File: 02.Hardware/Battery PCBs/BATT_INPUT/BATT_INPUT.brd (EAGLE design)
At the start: 26 x 30.6 mm, 39 parts, among them J1 70AAJ-4-M0, J4 DX07S016JA1R1500, U1 AT24C16D-STUM-T, U5 BQ24075, U9 Value

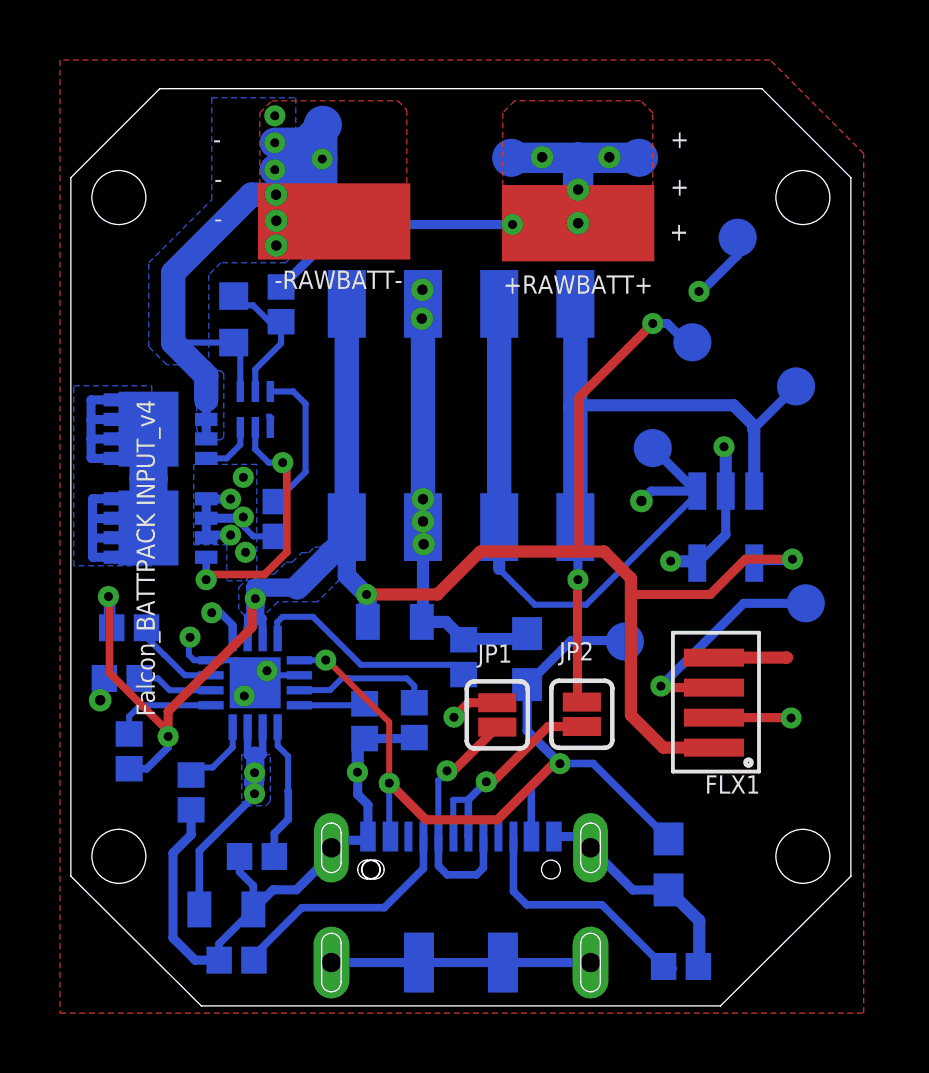
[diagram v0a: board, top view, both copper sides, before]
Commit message: Cambios revisados con David
Revision de los pcbs de la bateria.

En el DCDC se añade un diode Clamp (bat54s) en la medicion de la tension de salida.
Actualizacion de la BOM a v8.
Documentos de Cambios de versiones
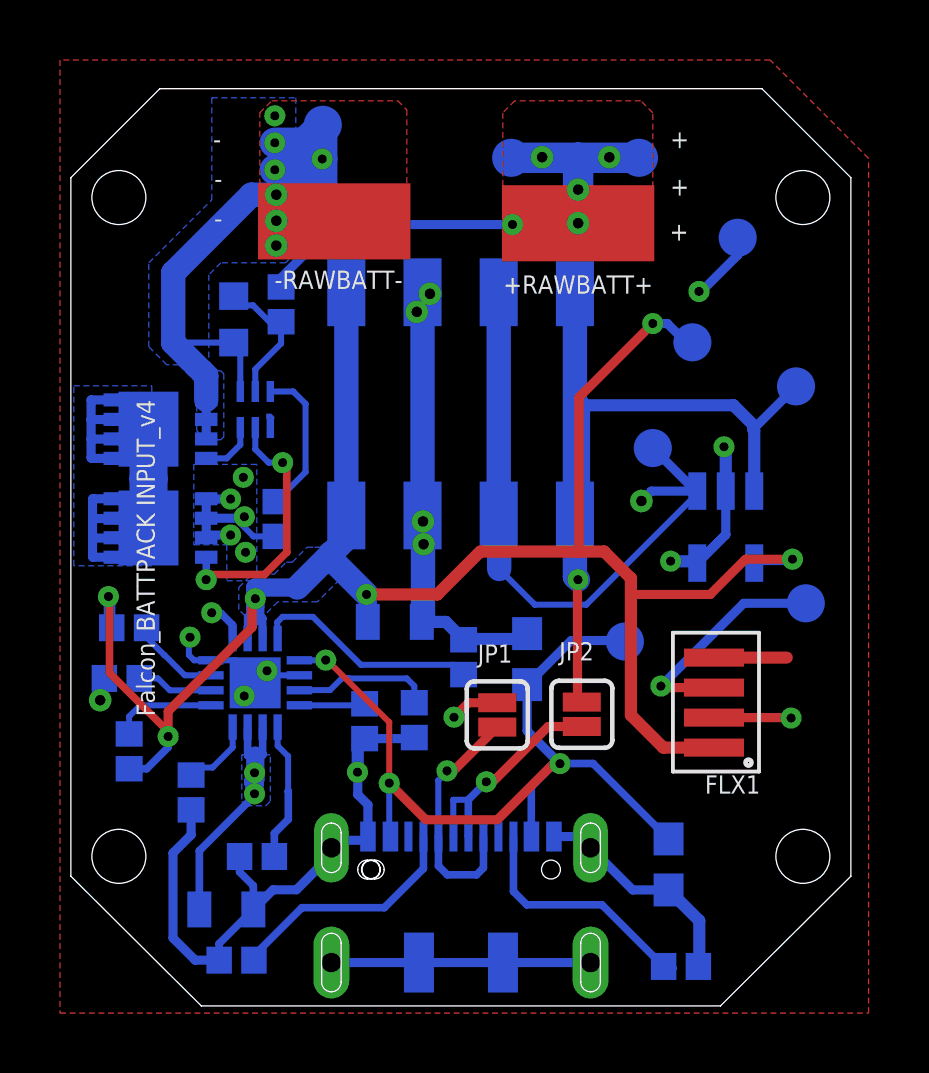
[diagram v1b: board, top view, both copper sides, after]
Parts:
- JP1, JP2: value JUMPER-SMT_2_NC_PASTE_SILK -> JUMPER-SMT_2_NO_SILK; device SparkFun-Jumpers:SMT-JUMPER_2_NC_PASTE_SILK -> SparkFun-Jumpers:SMT-JUMPER_2_NO_SILK
- moved J1 0.39 mm to (60.2, 57.2), turned to 180 degrees
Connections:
- net D+: now also J1.4, J1.5; no longer J1.1, J1.8
- net D-: now also J1.3, J1.6; no longer J1.2, J1.7
- net GND: now also J1.2, J1.7; no longer J1.3, J1.6
- net VSYS: now also J1.1, J1.8; no longer J1.4, J1.5
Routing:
- net D+: track 23.9 -> 30.0 mm
- net GND: track 73.9 -> 75.7 mm, vias 18 -> 17

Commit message: Review general antes de produccion
Se modifica:
R13 --> El sensado de vosense estaba tarado para 3.3v en vez de 3v de vsupply
R15 --> Se baja el valor porque  no hace falta que sea tan alta
C10 --> Error de valor 470n en vez de 47n
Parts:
- R1: value 1K1 -> 1K5
- R3: value 590 -> 909R
- R5: value 1K -> 100k
- U9: value Value -> BQ29700DSER
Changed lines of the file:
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@@
 <grid distance="0.002" unitdist="mm" unit="mm" style="lines" multiple="1" display="no" altdistance="5" altunitdist="mil" altunit="mil"/>
 <layers>
-<layer number="1" name="Top" color="4" fill="1" visible="yes" active="yes"/>
-<layer number="2" name="Route2" color="16" fill="1" visible="yes" active="yes"/>
+<layer number="1" name="Top" color="4" fill="1" visible="no" active="yes"/>
+<layer number="2" name="Route2" color="16" fill="1" visible="no" active="yes"/>
 <layer number="3" name="Route3" color="17" fill="1" visible="no" active="no"/>
 <layer number="4" name="Route4" color="18" fill="1" visible="no" active="no"/>
@@
 <layer number="20" name="Dimension" color="24" fill="1" visible="yes" active="yes"/>
 <layer number="21" name="tPlace" color="7" fill="1" visible="no" active="yes"/>
-<layer number="22" name="bPlace" color="7" fill="1" visible="no" active="yes"/>
+<layer number="22" name="bPlace" color="7" fill="1" visible="yes" active="yes"/>
 <layer number="23" name="tOrigins" color="15" fill="1" visible="yes" active="yes"/>
 <layer number="24" name="bOrigins" color="15" fill="1" visible="yes" active="yes"/>
-<layer number="25" name="tNames" color="7" fill="1" visible="no" active="yes"/>
+<layer number="25" name="tNames" color="7" fill="1" visible="yes" active="yes"/>
 <layer number="26" name="bNames" color="7" fill="1" visible="no" active="yes"/>
 <layer number="27" name="tValues" color="7" fill="1" visible="no" active="yes"/>
-<layer number="28" name="bValues" color="7" fill="1" visible="no" active="yes"/>
+<layer number="28" name="bValues" color="7" fill="1" visible="yes" active="yes"/>
 <layer number="29" name="tStop" color="7" fill="3" visible="no" active="yes"/>
 <layer number="30" name="bStop" color="7" fill="6" visible="no" active="yes"/>
@@
 <text x="73.07" y="62.014" size="0.6096" layer="26" font="vector" rot="MR270">Falcon_BATTPACK INPUT_v4</text>
 <text x="69.584" y="47.098" size="0.6096" layer="26" rot="MR270">July'21</text>
+<circle x="51.088" y="54.03" radius="0.101546875" width="0.1524" layer="22"/>
+<circle x="51.084" y="57.364" radius="0.09" width="0.1524" layer="22"/>
+<circle x="54.468" y="55.826" radius="0.106675" width="0.1524" layer="22"/>
 </plain>
 <attributes>
@@
 <attribute name="VENDOR" value="Texas Instruments" x="26.06" y="39.845" size="1.778" layer="28" rot="MR0" display="off"/>
 </element>
-<element name="R1" library="SparkFun-Resistors" package="0402" value="1K1" x="60.295" y="48.755" smashed="yes" rot="MR270">
+<element name="R1" library="SparkFun-Resistors" package="0402" value="1K5" x="60.295" y="48.755" smashed="yes" rot="MR270">
 <attribute name="NAME" x="60.365" y="50.3559" size="0.6096" layer="26" font="vector" rot="MR0" align="bottom-center"/>
 <attribute name="PROD_ID" value=" " x="60.295" y="48.755" size="1.778" layer="28" rot="MR270" display="off"/>
@@
 <attribute name="VALUE" value=" " x="52.7741" y="60.515" size="0.6096" layer="28" font="vector" rot="MR90" align="top-center"/>
 </element>
-<element name="R3" library="SparkFun-Resistors" package="0402" value="590" x="56.995" y="46.62" smashed="yes" rot="MR90">
+<element name="R3" library="SparkFun-Resistors" package="0402" value="909R" x="56.995" y="46.62" smashed="yes" rot="MR90">
 <attribute name="NAME" x="57" y="48.0299" size="0.6096" layer="26" font="vector" rot="MR0" align="bottom-center"/>
 <attribute name="PROD_ID" value=" " x="56.995" y="46.62" size="1.778" layer="28" rot="MR90" display="off"/>
@@
 <attribute name="PROD_ID" value="IC-13219" x="38.105" y="23.77" size="1.778" layer="28" rot="MR0" display="off"/>
 </element>
-<element name="U9" library="BQ2970" package="DSE0006A" value="Value" x="53.35" y="57.01" smashed="yes" rot="MR90">
+<element name="U9" library="BQ2970" package="DSE0006A" value="BQ29700DSER" x="53.35" y="57.01" smashed="yes" rot="MR90">
 <attribute name="MANUFACTURER" value="Texas Instruments" x="30.49" y="91.3" size="1.778" layer="28" rot="MR90" display="off"/>
 <attribute name="NAME" x="53.4626" y="55.291" size="0.6096" layer="26" font="vector" rot="SMR0"/>
@@
 <attribute name="PROD_ID" value=" " x="48.9" y="48.045" size="1.778" layer="28" rot="MR180" display="off"/>
 </element>
-<element name="R5" library="SparkFun-Resistors" package="0402" value="1K" x="49.145" y="49.735" smashed="yes" rot="MR0">
+<element name="R5" library="SparkFun-Resistors" package="0402" value="100k" x="49.145" y="49.735" smashed="yes" rot="MR0">
 <attribute name="NAME" x="49.914" y="50.4509" size="0.6096" layer="26" font="vector" rot="MR0" align="bottom-center"/>
 <attribute name="PROD_ID" value=" " x="49.145" y="49.735" size="1.778" layer="28" rot="MR0" display="off"/>
